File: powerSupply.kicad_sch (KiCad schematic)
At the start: 39 parts, among them SW2 PTS840_GK_SMTR_LFS, U10 MIC2877-5.0YFT-TR, U6 AP22652W6-7, U9 NCP1599MNTWG

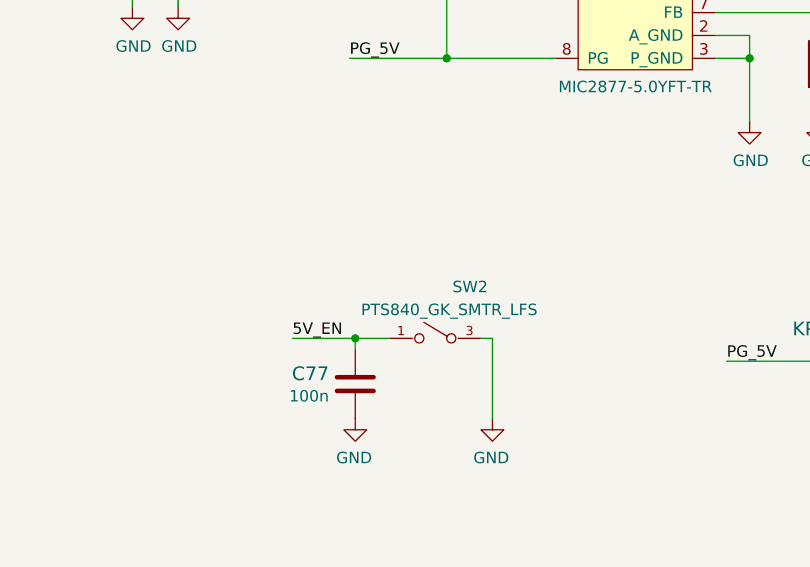
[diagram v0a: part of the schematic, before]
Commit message: Added FTDI schematic
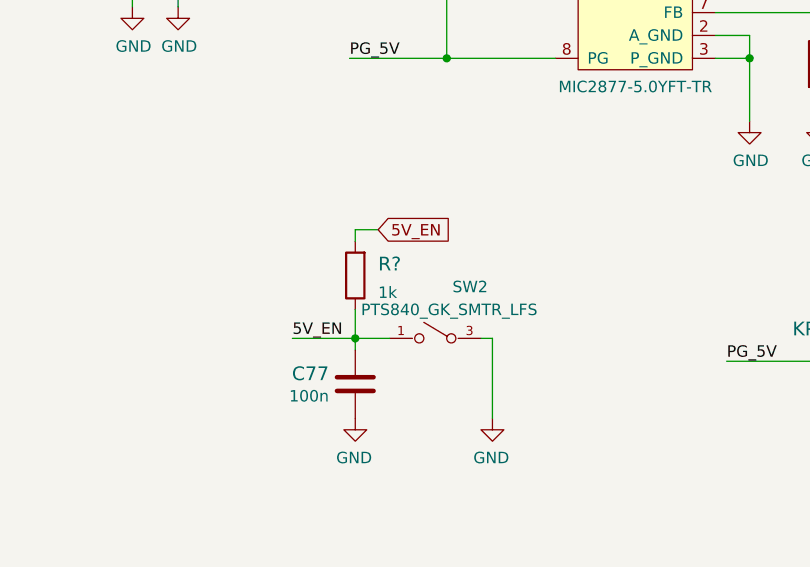
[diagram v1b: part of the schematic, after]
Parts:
- added R?: R_1k_0402, antmicro-footprints:0402-res, symbol antmicroResistors0402:R_1k_0402
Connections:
- net 5V_EN: now also R?.1, R?.2
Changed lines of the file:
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@@
+    (stroke (width 0) (type default) (color 0 0 0 0))
+  )
+  (wire (pts (xy 55.88 153.67) (xy 55.88 154.94))
     (stroke (width 0) (type default) (color 0 0 0 0))
   )
@@
     (stroke (width 0) (type default) (color 0 0 0 0))
   )
+  (wire (pts (xy 58.42 153.67) (xy 55.88 153.67))
+    (stroke (width 0) (type default) (color 0 0 0 0))
+  )
   (wire (pts (xy 69.215 118.11) (xy 69.215 116.84))
     (stroke (width 0) (type default) (color 0 0 0 0))
@@
     (stroke (width 0) (type default) (color 0 0 0 0))
   )
+  (wire (pts (xy 55.88 162.56) (xy 55.88 165.735))
+    (stroke (width 0) (type default) (color 0 0 0 0))
+  )
   (wire (pts (xy 158.115 127.635) (xy 158.115 130.175))
     (stroke (width 0) (type default) (color 0 0 0 0))
@@
     (stroke (width 0) (type default) (color 0 0 0 0))
   )
-  (wire (pts (xy 55.88 167.005) (xy 55.88 165.735))
+  (wire (pts (xy 55.88 165.735) (xy 55.88 167.005))
     (stroke (width 0) (type default) (color 0 0 0 0))
   )
@@
     (property "Intersheet References" "${INTERSHEET_REFS}" (id 0) (at 0 0 0)
       (effects (font (size 1.27 1.27)) hide)
+    )
+  )
+  (global_label "5V_EN" (shape input) (at 58.42 153.67 0) (fields_autoplaced)
+    (effects (font (size 1.27 1.27)) (justify left))
+    (property "Intersheet References" "${INTERSHEET_REFS}" (id 0) (at 66.4894 153.5906 0)
+      (effects (font (size 1.27 1.27)) (justify left) hide)
     )
   )
@@
     (pin "1")
   )
+  (symbol (lib_id "antmicroResistors0402:R_1k_0402") (at 55.88 158.75 90) (unit 1)
+    (in_bom yes) (on_board yes) (fields_autoplaced)
+    (property "Reference" "R?" (id 0) (at 58.42 157.48 90)
+      (effects (font (size 1.524 1.524)) (justify right))
+    )
+    (property "Value" "R_1k_0402" (id 1) (at 59.69 158.75 0)
+      (effects (font (size 1.524 1.524)) hide)
+    )
+    (property "Footprint" "antmicro-footprints:0402-res" (id 2) (at 50.8 153.67 0)
+      (effects (font (size 1.524 1.524)) (justify left) hide)
+    )
+    (property "Datasheet" "" (id 3) (at 55.88 158.75 0)
+      (effects (font (size 1.27 1.27)) hide)
+    )
+    (property "Manufacturer" "BOURNS" (id 4) (at 45.72 153.67 0)
+      (effects (font (size 1.524 1.524)) (justify left) hide)
+    )
+    (property "MPN" "CR0402-FX-1001GLF" (id 5) (at 48.26 153.67 0)
+      (effects (font (size 1.524 1.524)) (justify left) hide)
+    )
+    (property "Val" "1k" (id 6) (at 58.42 160.6549 90)
+      (effects (font (size 1.27 1.27)) (justify right))
+    )
+    (pin "1")
+    (pin "2")
+  )
 )

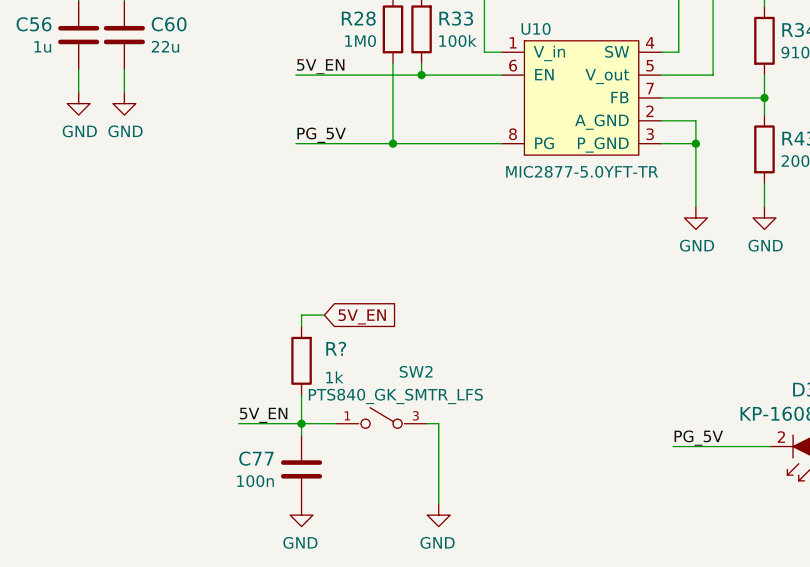
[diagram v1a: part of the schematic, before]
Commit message: Added comments to schematic
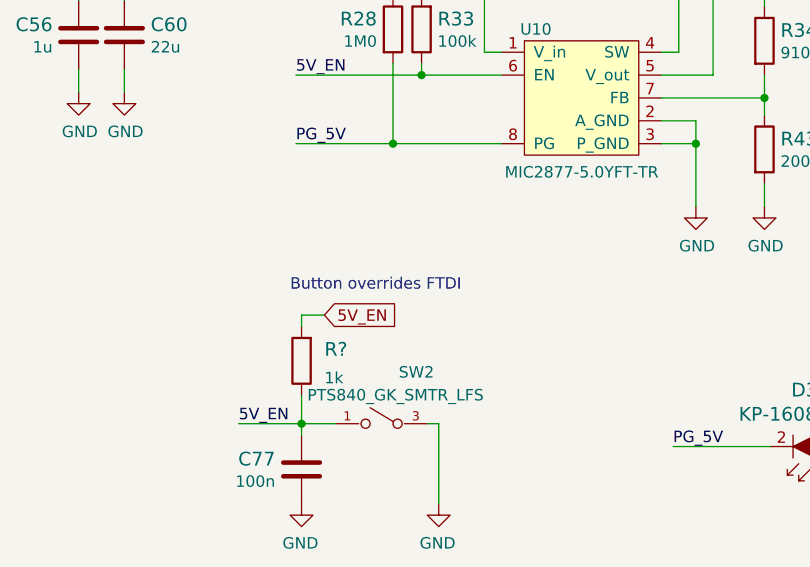
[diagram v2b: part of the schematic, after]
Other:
- note added: "Button overrides FTDI"
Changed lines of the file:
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@@
     (stroke (width 0) (type default) (color 0 0 0 0))
+  )
+  (text "Button overrides FTDI" (at 54.61 151.13 0)
+    (effects (font (size 1.27 1.27)) (justify left bottom))
   )
   (text "Note: ILIM - R17k4 \nlimit current to 1.018A" (at 301.625 64.135 0)

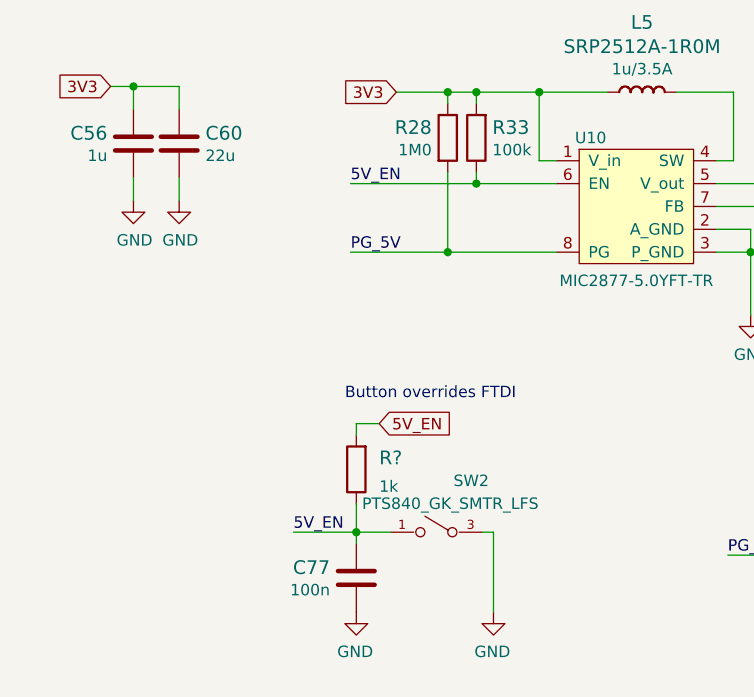
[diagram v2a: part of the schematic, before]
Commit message: Created FT2232 layout
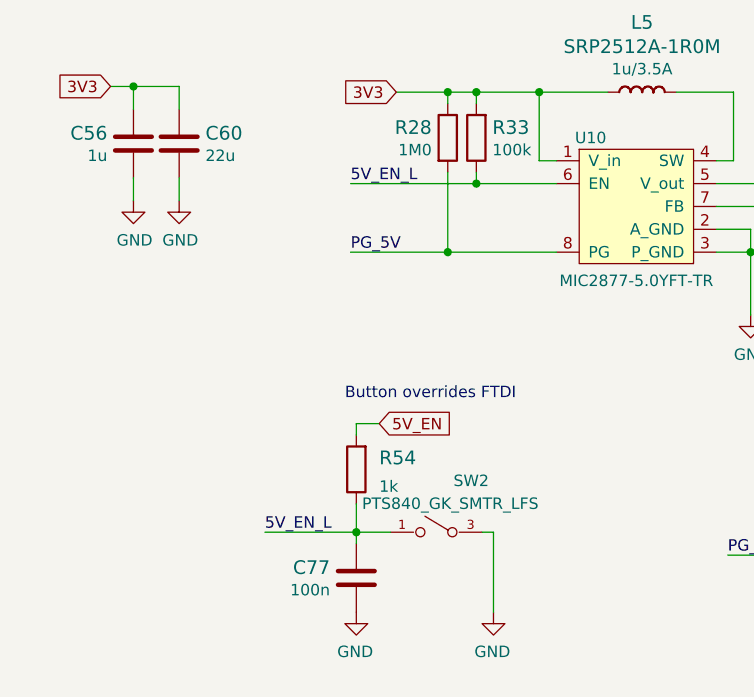
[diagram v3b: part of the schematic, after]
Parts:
- SW2: DNP (none) -> DNP
- gave numbers to parts that had none: 1
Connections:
- net 5V_EN: no longer C77.1, R33.1, R54.1, SW2.1, SW2.2, U10.6 (EN)
- new net 5V_EN_L: C77.1, R33.1, R54.1, SW2.1, SW2.2, U10.6 (EN)
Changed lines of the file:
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@@
   (title_block
     (title "M.2 Smart IoT Module")
-    (date "2021-08-11")
-    (rev "1.1.0")
+    (date "2022-07-11")
+    (rev "1.2.0")
     (comment 1 "www.antmicro.com")
     (comment 2 "Antmicro Ltd.")
@@
     (stroke (width 0) (type default) (color 0 0 0 0))
   )
-  (wire (pts (xy 48.895 165.735) (xy 55.88 165.735))
+  (wire (pts (xy 45.72 165.735) (xy 55.88 165.735))
     (stroke (width 0) (type default) (color 0 0 0 0))
   )
@@
     (effects (font (size 1.27 1.27)) (justify left bottom))
   )
-  (label "5V_EN" (at 55.245 127 0)
+  (label "5V_EN_L" (at 55.245 127 0)
     (effects (font (size 1.27 1.27)) (justify left bottom))
   )
@@
     (effects (font (size 1.27 1.27)) (justify left bottom))
   )
-  (label "5V_EN" (at 48.895 165.735 0)
+  (label "5V_EN_L" (at 45.72 165.735 0)
     (effects (font (size 1.27 1.27)) (justify left bottom))
   )
@@
       (effects (font (size 1.27 1.27)) hide)
     )
+    (property "DNP" "DNP" (id 6) (at 69.85 160.655 0)
+      (effects (font (size 1.27 1.27)) hide)
+    )
     (pin "1")
     (pin "2")
@@
   (symbol (lib_id "antmicroResistors0402:R_1k_0402") (at 55.88 158.75 90) (unit 1)
     (in_bom yes) (on_board yes) (fields_autoplaced)
-    (property "Reference" "R?" (id 0) (at 58.42 157.48 90)
+    (property "Reference" "R54" (id 0) (at 58.42 157.48 90)
       (effects (font (size 1.524 1.524)) (justify right))
     )

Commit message: Applied fixes to issues that came up in review
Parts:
- removed R33: R_100k_0402, m2-smart-iot-module-footprints:0402-res, symbol m2-smart-iot-module:R_100k_0402
- added R33: R_200k_0402, antmicro-footprints:0402-res, symbol antmicroResistors0402:R_200k_0402
- added R62: R_10k_0402, antmicro-footprints:0402-res, symbol antmicroResistors0402:R_10k_0402
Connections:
- net 3V3: now also R62.2
- net 5V_EN_L: now also R33.1; no longer C77.1, R54.1, SW2.1, SW2.2
- new net: C77.1, R33.2, R54.1, R62.1, SW2.1, SW2.2
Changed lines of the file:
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@@
   (junction (at 66.04 50.8) (diameter 0) (color 0 0 0 0)
   )
-  (junction (at 69.215 127) (diameter 0) (color 0 0 0 0)
-  )
   (junction (at 102.87 63.5) (diameter 0) (color 0 0 0 0)
   )
@@
   (junction (at 267.97 52.07) (diameter 0) (color 0 0 0 0)
   )
+  (junction (at 45.72 165.735) (diameter 0) (color 0 0 0 0)
+  )
   (junction (at 147.32 62.865) (diameter 0) (color 0 0 0 0)
   )
@@
   (junction (at 99.695 134.62) (diameter 0) (color 0 0 0 0)
   )
-  (junction (at 69.215 116.84) (diameter 0) (color 0 0 0 0)
-  )
   (junction (at 358.775 61.595) (diameter 0) (color 0 0 0 0)
   )
@@
     (stroke (width 0) (type default) (color 0 0 0 0))
   )
+  (wire (pts (xy 45.72 165.735) (xy 55.88 165.735))
+    (stroke (width 0) (type default) (color 0 0 0 0))
+  )
   (wire (pts (xy 55.88 153.67) (xy 55.88 154.94))
     (stroke (width 0) (type default) (color 0 0 0 0))
@@
     (stroke (width 0) (type default) (color 0 0 0 0))
   )
-  (wire (pts (xy 69.215 118.11) (xy 69.215 116.84))
-    (stroke (width 0) (type default) (color 0 0 0 0))
-  )
   (wire (pts (xy 83.82 116.84) (xy 76.2 116.84))
     (stroke (width 0) (type default) (color 0 0 0 0))
@@
     (stroke (width 0) (type default) (color 0 0 0 0))
   )
+  (wire (pts (xy 45.72 162.56) (xy 45.72 165.735))
+    (stroke (width 0) (type default) (color 0 0 0 0))
+  )
   (wire (pts (xy 259.715 54.61) (xy 258.445 54.61))
     (stroke (width 0) (type default) (color 0 0 0 0))
@@
     (stroke (width 0) (type default) (color 0 0 0 0))
   )
-  (wire (pts (xy 69.215 127) (xy 78.105 127))
+  (wire (pts (xy 68.58 127) (xy 78.105 127))
     (stroke (width 0) (type default) (color 0 0 0 0))
   )
@@
     (stroke (width 0) (type default) (color 0 0 0 0))
   )
-  (wire (pts (xy 45.72 165.735) (xy 55.88 165.735))
+  (wire (pts (xy 43.815 165.735) (xy 45.72 165.735))
     (stroke (width 0) (type default) (color 0 0 0 0))
   )
@@
     (stroke (width 0) (type default) (color 0 0 0 0))
   )
+  (wire (pts (xy 45.72 153.67) (xy 45.72 154.94))
+    (stroke (width 0) (type default) (color 0 0 0 0))
+  )
   (wire (pts (xy 137.16 62.865) (xy 147.32 62.865))
     (stroke (width 0) (type default) (color 0 0 0 0))
@@
     (stroke (width 0) (type default) (color 0 0 0 0))
   )
+  (wire (pts (xy 44.45 153.67) (xy 45.72 153.67))
+    (stroke (width 0) (type default) (color 0 0 0 0))
+  )
   (wire (pts (xy 147.955 132.08) (xy 147.955 130.175))
     (stroke (width 0) (type default) (color 0 0 0 0))
@@
     (stroke (width 0) (type default) (color 0 0 0 0))
   )
-  (wire (pts (xy 66.04 116.84) (xy 69.215 116.84))
+  (wire (pts (xy 66.04 116.84) (xy 76.2 116.84))
     (stroke (width 0) (type default) (color 0 0 0 0))
   )
@@
     (stroke (width 0) (type default) (color 0 0 0 0))
   )
-  (wire (pts (xy 69.215 127) (xy 55.245 127))
-    (stroke (width 0) (type default) (color 0 0 0 0))
-  )
   (wire (pts (xy 157.48 62.865) (xy 157.48 60.96))
     (stroke (width 0) (type default) (color 0 0 0 0))
@@
     (stroke (width 0) (type default) (color 0 0 0 0))
   )
-  (wire (pts (xy 69.215 116.84) (xy 76.2 116.84))
-    (stroke (width 0) (type default) (color 0 0 0 0))
-  )
   (wire (pts (xy 99.695 132.08) (xy 95.885 132.08))
     (stroke (width 0) (type default) (color 0 0 0 0))
@@
     (stroke (width 0) (type default) (color 0 0 0 0))
   )
+  (wire (pts (xy 26.67 165.735) (xy 36.195 165.735))
+    (stroke (width 0) (type default) (color 0 0 0 0))
+  )
   (wire (pts (xy 59.69 228.6) (xy 76.2 228.6))
     (stroke (width 0) (type default) (color 0 0 0 0))
@@
   )
   (wire (pts (xy 107.315 127) (xy 107.315 129.54))
-    (stroke (width 0) (type default) (color 0 0 0 0))
-  )
-  (wire (pts (xy 69.215 125.73) (xy 69.215 127))
     (stroke (width 0) (type default) (color 0 0 0 0))
   )
@@
     (effects (font (size 1.27 1.27)) (justify left bottom))
   )
-  (label "5V_EN_L" (at 55.245 127 0)
+  (label "5V_EN_L" (at 68.58 127 0)
     (effects (font (size 1.27 1.27)) (justify left bottom))
   )
@@
     (effects (font (size 1.27 1.27)) (justify left bottom))
   )
-  (label "5V_EN_L" (at 45.72 165.735 0)
+  (label "5V_EN_L" (at 26.67 165.735 0)
     (effects (font (size 1.27 1.27)) (justify left bottom))
   )
@@
     (effects (font (size 1.27 1.27)) (justify right))
     (property "Intersheet References" "${INTERSHEET_REFS}" (id 0) (at 0 0 0)
+      (effects (font (size 1.27 1.27)) hide)
+    )
+  )
+  (global_label "3V3" (shape input) (at 44.45 153.67 180) (fields_autoplaced)
+    (effects (font (size 1.27 1.27)) (justify right))
+    (property "Intersheet References" "${INTERSHEET_REFS}" (id 0) (at -15.875 36.83 0)
       (effects (font (size 1.27 1.27)) hide)
     )
@@
     (pin "2")
   )
-  (symbol (lib_id "m2-smart-iot-module:R_100k_0402") (at 69.215 121.92 90) (unit 1)
-    (in_bom yes) (on_board yes)
-    (property "Reference" "R33" (id 0) (at 70.993 120.777 90)
-      (effects (font (size 1.524 1.524)) (justify right))
-    )
-    (property "Value" "R_100k_0402" (id 1) (at 73.025 121.92 0)
-      (effects (font (size 1.524 1.524)) hide)
-    )
-    (property "Footprint" "m2-smart-iot-module-footprints:0402-res" (id 2) (at 64.135 116.84 0)
-      (effects (font (size 1.524 1.524)) (justify left) hide)
-    )
-    (property "Datasheet" "" (id 3) (at 69.215 121.92 0)
-      (effects (font (size 1.27 1.27)) hide)
-    )
-    (property "Manufacturer" "VISHAY" (id 4) (at 59.055 116.84 0)
-      (effects (font (size 1.524 1.524)) (justify left) hide)
-    )
-    (property "MPN" "CRCW0402100KFKEDHP" (id 5) (at 61.595 116.84 0)
-      (effects (font (size 1.524 1.524)) (justify left) hide)
-    )
-    (property "Val" "100k" (id 6) (at 70.993 123.2662 90)
-      (effects (font (size 1.27 1.27)) (justify right))
-    )
-    (pin "1")
-    (pin "2")
-  )
   (symbol (lib_id "m2-smart-iot-module:R_200k_0402") (at 107.315 135.255 270) (unit 1)
     (in_bom yes) (on_board yes)
@@
       (effects (font (size 1.27 1.27)) (justify right))
     )
+    (pin "1")
+    (pin "2")
+  )
+  (symbol (lib_id "antmicroResistors0402:R_200k_0402") (at 40.005 165.735 0) (unit 1)
+    (in_bom yes) (on_board yes) (fields_autoplaced)
+    (property "Reference" "R33" (id 0) (at 40.005 158.75 0)
+      (effects (font (size 1.524 1.524)))
+    )
+    (property "Value" "R_200k_0402" (id 1) (at 40.005 169.545 0)
+      (effects (font (size 1.524 1.524)) hide)
+    )
+    (property "Footprint" "antmicro-footprints:0402-res" (id 2) (at 45.085 160.655 0)
+      (effects (font (size 1.524 1.524)) (justify left) hide)
+    )
+    (property "Datasheet" "" (id 3) (at 40.005 165.735 0)
+      (effects (font (size 1.27 1.27)) hide)
+    )
+    (property "Manufacturer" "YAGEO_(PHYCOMP)" (id 4) (at 45.085 155.575 0)
+      (effects (font (size 1.524 1.524)) (justify left) hide)
+    )
+    (property "MPN" "RC0402FR-07200KL" (id 5) (at 45.085 158.115 0)
+      (effects (font (size 1.524 1.524)) (justify left) hide)
+    )
+    (property "Val" "200k" (id 6) (at 40.005 162.56 0))
+    (pin "1")
+    (pin "2")
+  )
+  (symbol (lib_id "antmicroResistors0402:R_10k_0402") (at 45.72 158.75 90) (unit 1)
+    (in_bom yes) (on_board yes) (fields_autoplaced)
+    (property "Reference" "R62" (id 0) (at 48.26 157.48 90)
+      (effects (font (size 1.524 1.524)) (justify right))
+    )
+    (property "Value" "R_10k_0402" (id 1) (at 49.53 158.75 0)
+      (effects (font (size 1.524 1.524)) hide)
+    )
+    (property "Footprint" "antmicro-footprints:0402-res" (id 2) (at 40.64 153.67 0)
+      (effects (font (size 1.524 1.524)) (justify left) hide)
+    )
+    (property "Datasheet" "" (id 3) (at 45.72 158.75 0)
+      (effects (font (size 1.27 1.27)) hide)
+    )
+    (property "Manufacturer" "VISHAY" (id 4) (at 35.56 153.67 0)
+      (effects (font (size 1.524 1.524)) (justify left) hide)
+    )
+    (property "MPN" "CRCW040210K0FKEDHP" (id 5) (at 38.1 153.67 0)
+      (effects (font (size 1.524 1.524)) (justify left) hide)
+    )
+    (property "Val" "10k" (id 6) (at 48.26 160.6549 90)
+      (effects (font (size 1.27 1.27)) (justify right))
+    )
